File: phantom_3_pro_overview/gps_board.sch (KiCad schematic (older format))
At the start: 0 parts

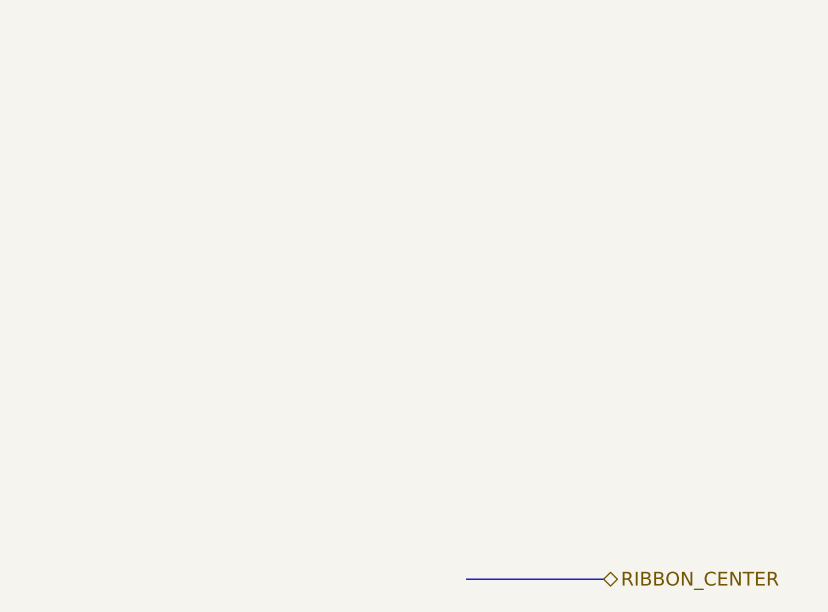
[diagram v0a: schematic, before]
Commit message: Overview: Conceptual schematics of some components.
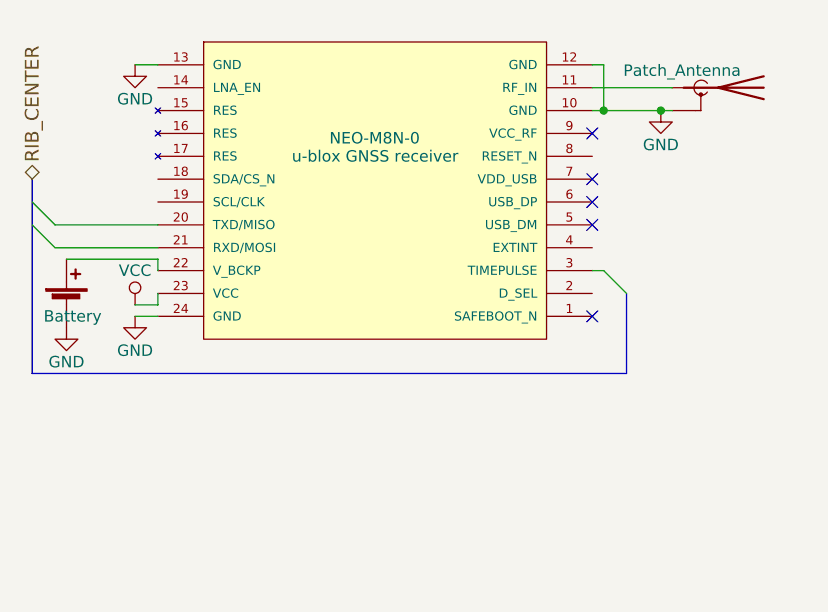
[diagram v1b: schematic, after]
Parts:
- added AE?: Patch_Antenna, symbol Antenna_Shield
- added BT?: Battery, symbol Battery_Cell
- added MODULE?: NEO-M8N-0, u-blox GNSS receiver, symbol GPS-NEO-M8
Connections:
- new net: AE?.1 (A), MODULE?.11 (RF_IN)
- new net: BT?.1 (+), MODULE?.22 (V_BCKP)
- new net GND: AE?.2 (Shield), BT?.2 (-), MODULE?.10 (GND), MODULE?.12 (GND), MODULE?.13 (GND), MODULE?.24 (GND)
- new net VCC: MODULE?.23 (VCC)
- no-connect marks 0 -> 5
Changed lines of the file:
@@
 LIBS:valves
 LIBS:motors
+LIBS:ic_dil_generic
+LIBS:sensors
+LIBS:u-blox
+LIBS:amplifiers
 LIBS:phantom_3_pro_overview-cache
 EELAYER 25 0
 EELAYER END
-$Descr A4 11693 8268
+$Descr User 5197 4000
 encoding utf-8
-Sheet 10 23
-Title ""
+Sheet 7 23
+Title "Overview of the Phantom 3 Pro GPS board"
 Date ""
 Rev ""
 Comp ""
-Comment1 ""
+Comment1 "This schematic does not aim to be electrically correct, it is conceptual."
 Comment2 ""
 Comment3 ""
 Comment4 ""
 $EndDescr
+Text HLabel 1100 1200 1    60   BiDi ~ 0
+RIB_CENTER
+$Comp
+L Antenna_Shield AE?
+U 1 1 596E99A2
+P 4100 800
+F 0 "AE?" H 4025 975 50  0001 R CNN
+F 1 "Patch_Antenna" V 4025 900 50  0000 R CNN
+F 2 "" H 4100 900 50  0001 C CNN
+F 3 "" H 4100 900 50  0001 C CNN
+	1    4100 800
+	0    1    1    0
+$EndComp
+$Comp
+L GPS-NEO-M8 MODULE?
+U 1 1 596EA877
+P 2600 1250
+F 0 "MODULE?" H 1850 1900 50  0001 L BNN
+F 1 "NEO-M8N-0" H 2400 1450 50  0000 L BNN
+F 2 "u-blox GNSS receiver" H 2600 1400 50  0000 C CNN
+F 3 "" H 2600 1250 60  0001 C CNN
+	1    2600 1250
+	1    0    0    -1
+$EndComp
+$Comp
+L GND #PWR?
+U 1 1 596EAAE6
+P 1550 1800
+F 0 "#PWR?" H 1550 1550 50  0001 C CNN
+F 1 "GND" H 1550 1650 50  0000 C CNN
+F 2 "" H 1550 1800 50  0001 C CNN
+F 3 "" H 1550 1800 50  0001 C CNN
+	1    1550 1800
+	1    0    0    -1
+$EndComp
+Entry Wire Line
+	1100 1300 1200 1400
+Entry Wire Line
+	1100 1400 1200 1500
+$Comp
+L GND #PWR?
+U 1 1 596EAB6F
+P 3850 900
+F 0 "#PWR?" H 3850 650 50  0001 C CNN
+F 1 "GND" H 3850 750 50  0000 C CNN
+F 2 "" H 3850 900 50  0001 C CNN
+F 3 "" H 3850 900 50  0001 C CNN
+	1    3850 900
+	1    0    0    -1
+$EndComp
+$Comp
+L GND #PWR?
+U 1 1 596EAB85
+P 1550 700
+F 0 "#PWR?" H 1550 450 50  0001 C CNN
+F 1 "GND" H 1550 550 50  0000 C CNN
+F 2 "" H 1550 700 50  0001 C CNN
+F 3 "" H 1550 700 50  0001 C CNN
+	1    1550 700
+	1    0    0    -1
+$EndComp
+Entry Wire Line
+	3600 1600 3700 1700
+NoConn ~ 3550 1000
+NoConn ~ 3550 1800
+$Comp
+L Battery_Cell BT?
+U 1 1 596EAD40
+P 1250 1750
+F 0 "BT?" H 1350 1850 50  0001 L CNN
+F 1 "Battery" H 1150 1700 50  0000 L CNN
+F 2 "" V 1250 1810 50  0001 C CNN
+F 3 "" V 1250 1810 50  0001 C CNN
+	1    1250 1750
+	1    0    0    -1
+$EndComp
+$Comp
+L GND #PWR?
+U 1 1 596EAFAF
+P 1250 1850
+F 0 "#PWR?" H 1250 1600 50  0001 C CNN
+F 1 "GND" H 1250 1700 50  0000 C CNN
+F 2 "" H 1250 1850 50  0001 C CNN
+F 3 "" H 1250 1850 50  0001 C CNN
+	1    1250 1850
+	1    0    0    -1
+$EndComp
+$Comp
+L VCC #PWR?
+U 1 1 596EAAD2
+P 1550 1750
+F 0 "#PWR?" H 1550 1600 50  0001 C CNN
+F 1 "VCC" H 1550 1900 50  0000 C CNN
+F 2 "" H 1550 1750 50  0001 C CNN
+F 3 "" H 1550 1750 50  0001 C CNN
+	1    1550 1750
+	1    0    0    -1
+$EndComp
+Wire Wire Line
+	3550 800  3900 800
+Wire Wire Line
+	3550 900  3900 900
+Wire Wire Line
+	3550 700  3600 700
+Wire Wire Line
+	3600 700  3600 900
+Connection ~ 3600 900
+Wire Wire Line
+	1200 1400 1650 1400
+Wire Wire Line
+	1200 1500 1650 1500
 Wire Bus Line
-	3000 2950 3600 2950
-Text HLabel 3600 2950 2    60   BiDi ~ 0
-RIBBON_CENTER
+	1100 1200 1100 2050
+Connection ~ 3850 900
+Wire Wire Line
+	1550 700  1650 700
+Wire Bus Line
+	3700 1700 3700 2050
+Wire Wire Line
+	3550 1600 3600 1600
+Wire Wire Line
+	1650 1550 1650 1600
+Wire Wire Line
+	1650 1750 1650 1700
+Wire Wire Line
+	1250 1550 1650 1550
+Wire Wire Line
+	1550 1750 1650 1750
+Wire Wire Line
+	1550 1800 1650 1800
+Wire Bus Line
+	3700 2050 1100 2050
+NoConn ~ 3550 1200
+NoConn ~ 3550 1300
+NoConn ~ 3550 1400
 $EndSCHEMATC

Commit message: Overview: Upgraded to KiCAD 5.0.1.
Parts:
- AE?: symbol Antenna_Shield -> Device:Antenna_Shield
- BT?: symbol Battery_Cell -> Device:Battery_Cell
- MODULE?: symbol GPS-NEO-M8 -> u-blox:GPS-NEO-M8
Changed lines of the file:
@@
-EESchema Schematic File Version 2
-LIBS:power
-LIBS:device
-LIBS:transistors
-LIBS:conn
-LIBS:linear
-LIBS:regul
-LIBS:74xx
-LIBS:cmos4000
-LIBS:adc-dac
-LIBS:memory
-LIBS:xilinx
-LIBS:microcontrollers
-LIBS:dsp
-LIBS:microchip
-LIBS:analog_switches
-LIBS:motorola
-LIBS:texas
-LIBS:intel
-LIBS:audio
-LIBS:interface
-LIBS:digital-audio
-LIBS:philips
-LIBS:display
-LIBS:cypress
-LIBS:siliconi
-LIBS:opto
-LIBS:atmel
-LIBS:contrib
-LIBS:valves
-LIBS:motors
-LIBS:ic_dil_generic
-LIBS:sensors
-LIBS:u-blox
-LIBS:amplifiers
-LIBS:transistors-switches
-LIBS:transistors-power
-LIBS:sensors-v2
-LIBS:regul-v2
+EESchema Schematic File Version 4
 LIBS:phantom_3_pro_overview-cache
-EELAYER 25 0
+EELAYER 26 0
 EELAYER END
 $Descr User 5197 4000
@@
 RIB_CENTER
 $Comp
-L Antenna_Shield AE?
+L Device:Antenna_Shield AE?
 U 1 1 596E99A2
 P 4100 800
@@
 $EndComp
 $Comp
-L GPS-NEO-M8 MODULE?
+L u-blox:GPS-NEO-M8 MODULE?
 U 1 1 596EA877
 P 2600 1250
@@
 $EndComp
 $Comp
-L GND #PWR?
+L power:GND #PWR?
 U 1 1 596EAAE6
 P 1550 1800
@@
 	1100 1400 1200 1500
 $Comp
-L GND #PWR?
+L power:GND #PWR?
 U 1 1 596EAB6F
 P 3850 900
@@
 $EndComp
 $Comp
-L GND #PWR?
+L power:GND #PWR?
 U 1 1 596EAB85
 P 1550 700
@@
 NoConn ~ 3550 1800
 $Comp
-L Battery_Cell BT?
+L Device:Battery_Cell BT?
 U 1 1 596EAD40
 P 1250 1750
@@
 $EndComp
 $Comp
-L GND #PWR?
+L power:GND #PWR?
 U 1 1 596EAFAF
 P 1250 1850
@@
 $EndComp
 $Comp
-L VCC #PWR?
+L power:VCC #PWR?
 U 1 1 596EAAD2
 P 1550 1750

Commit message: All: Finished updating to KiCad 5.0.1.
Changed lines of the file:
@@
 	3550 800  3900 800
 Wire Wire Line
-	3550 900  3900 900
+	3550 900  3600 900
 Wire Wire Line
 	3550 700  3600 700
@@
 Wire Wire Line
 	1200 1500 1650 1500
-Wire Bus Line
-	1100 1200 1100 2050
 Connection ~ 3850 900
 Wire Wire Line
@@
 NoConn ~ 3550 1300
 NoConn ~ 3550 1400
+Wire Wire Line
+	3600 900  3850 900
+Wire Wire Line
+	3850 900  3900 900
+Wire Bus Line
+	1100 1200 1100 2050
 $EndSCHEMATC
